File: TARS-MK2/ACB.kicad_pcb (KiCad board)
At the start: 2 copper layers, 69.9 x 162.4 mm, 43 parts, among them IC101 MP2384GG-P, J201 2309413-1, Q201 DMN2230U, U201 TLV70018_SOT23-5

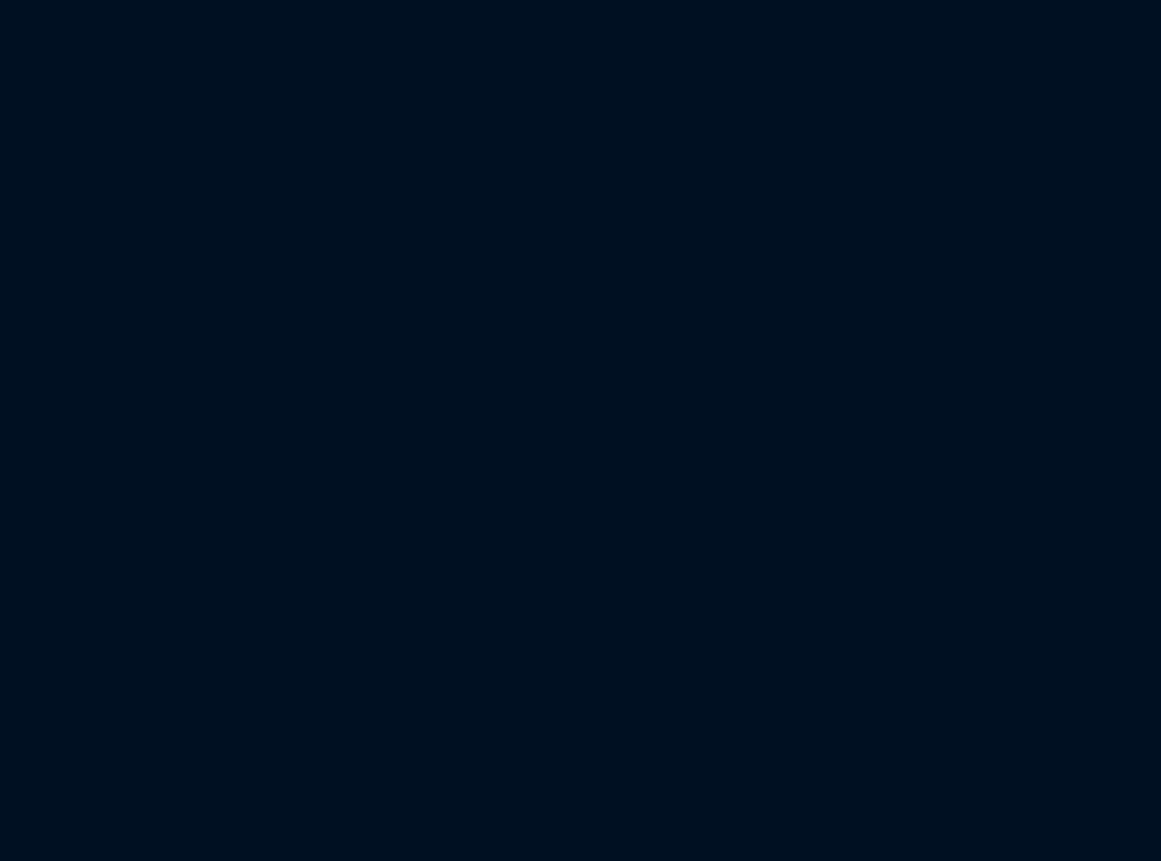
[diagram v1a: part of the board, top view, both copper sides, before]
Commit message: PT+SLND connections + various tweaks
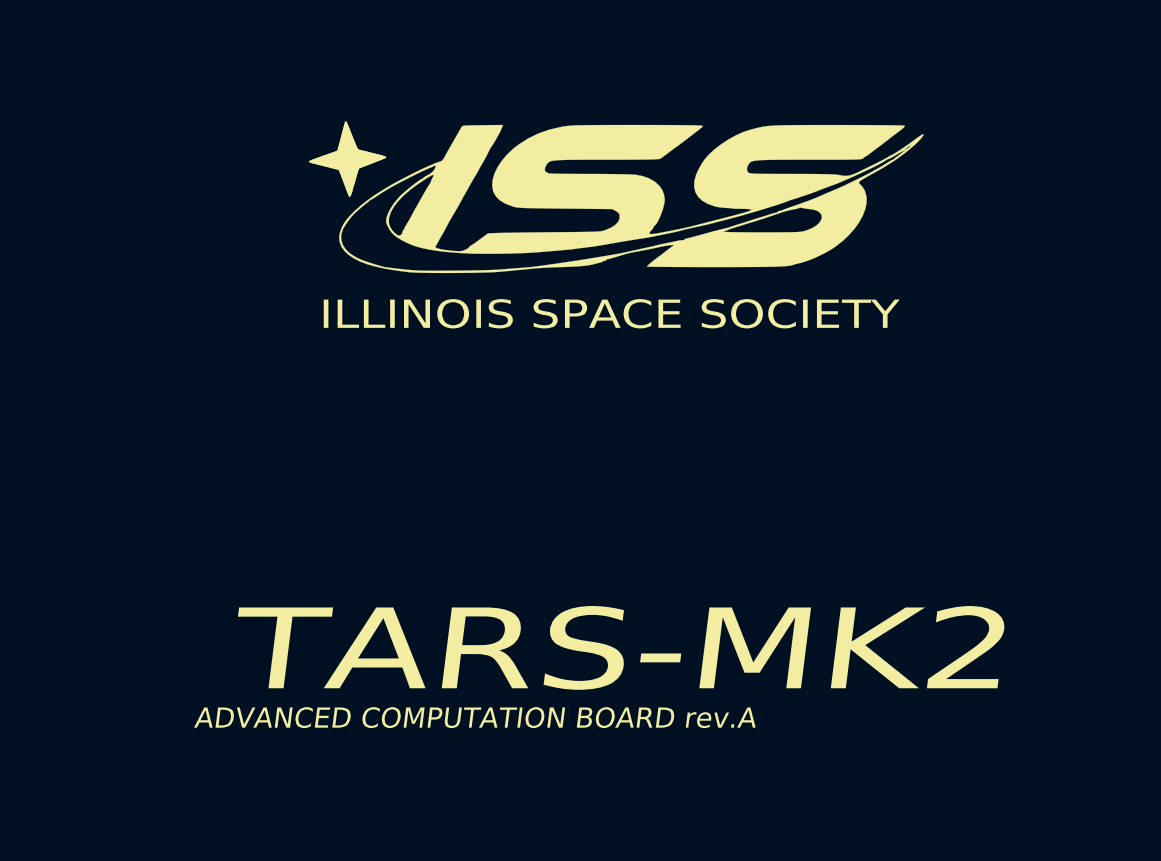
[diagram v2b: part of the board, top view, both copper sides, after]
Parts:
- added G***: LOGO, ISS_LOGO:ISS_LOGOV2_smaller, F.Cu at (287.8, 188.4)
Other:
- board text added: "ADVANCED COMPUTATION BOARD rev.A"
- board text added: "TARS-MK2"
